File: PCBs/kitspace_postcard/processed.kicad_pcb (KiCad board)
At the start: 2 copper layers, 100 x 100 mm, 23 parts, among them SW1 SW_Push, U1 ATtiny85-20SU

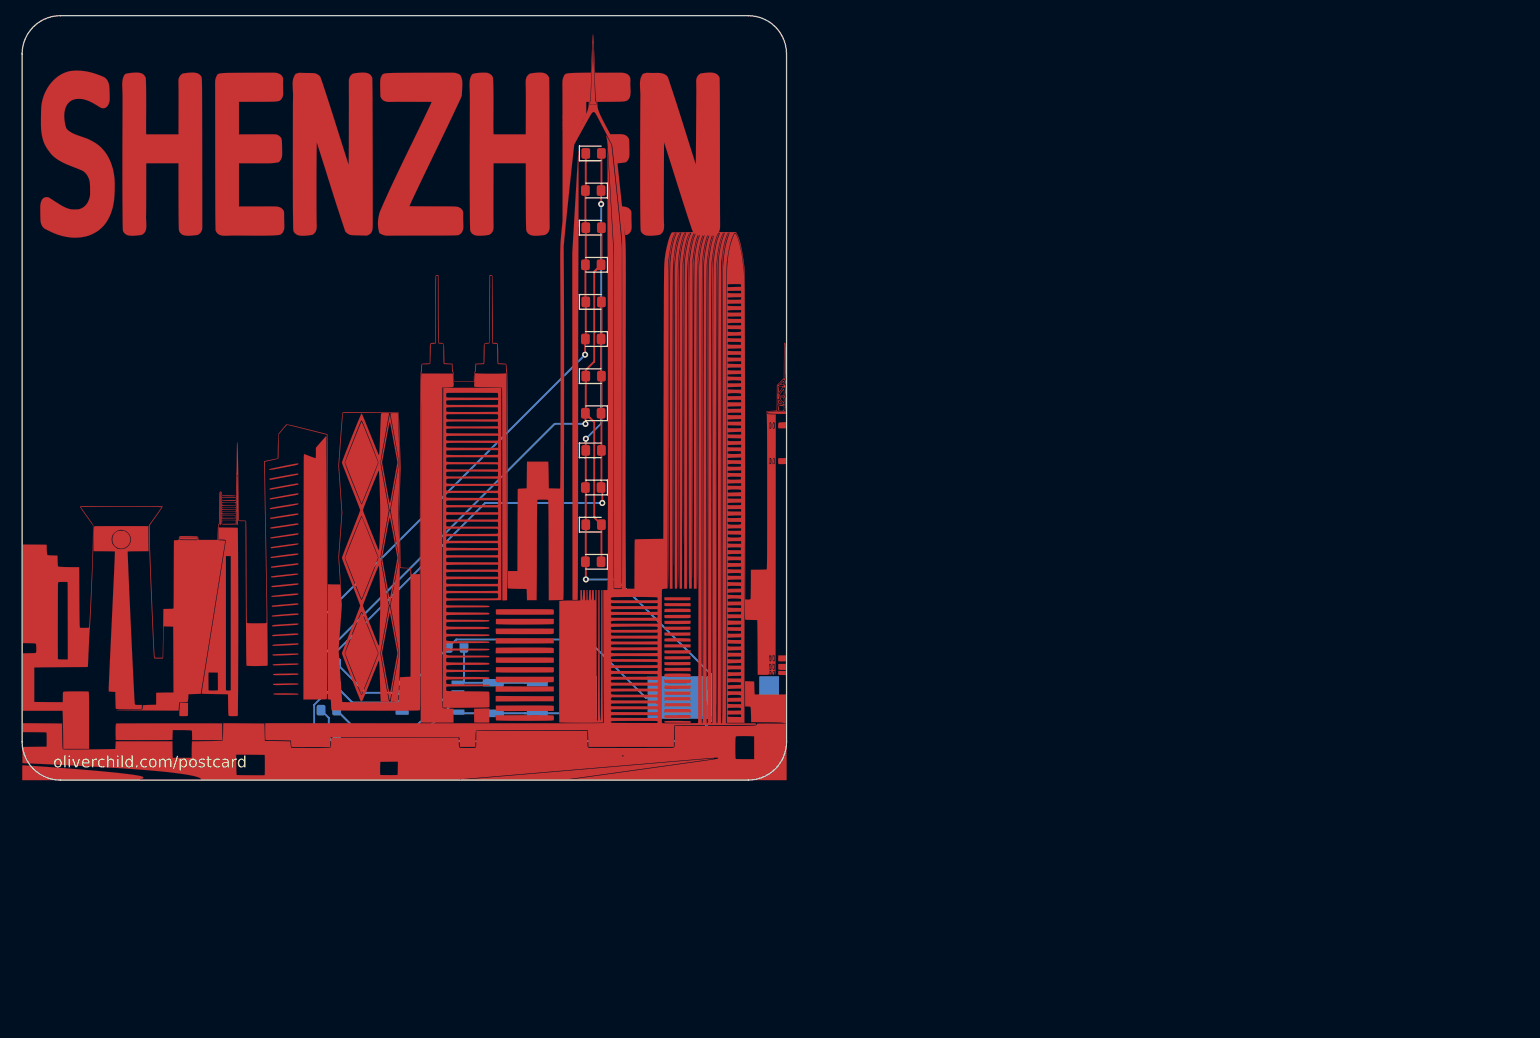
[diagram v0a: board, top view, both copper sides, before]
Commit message: recheck all circuits and clean up fill zone by rerouting the nets using freerouting and manually
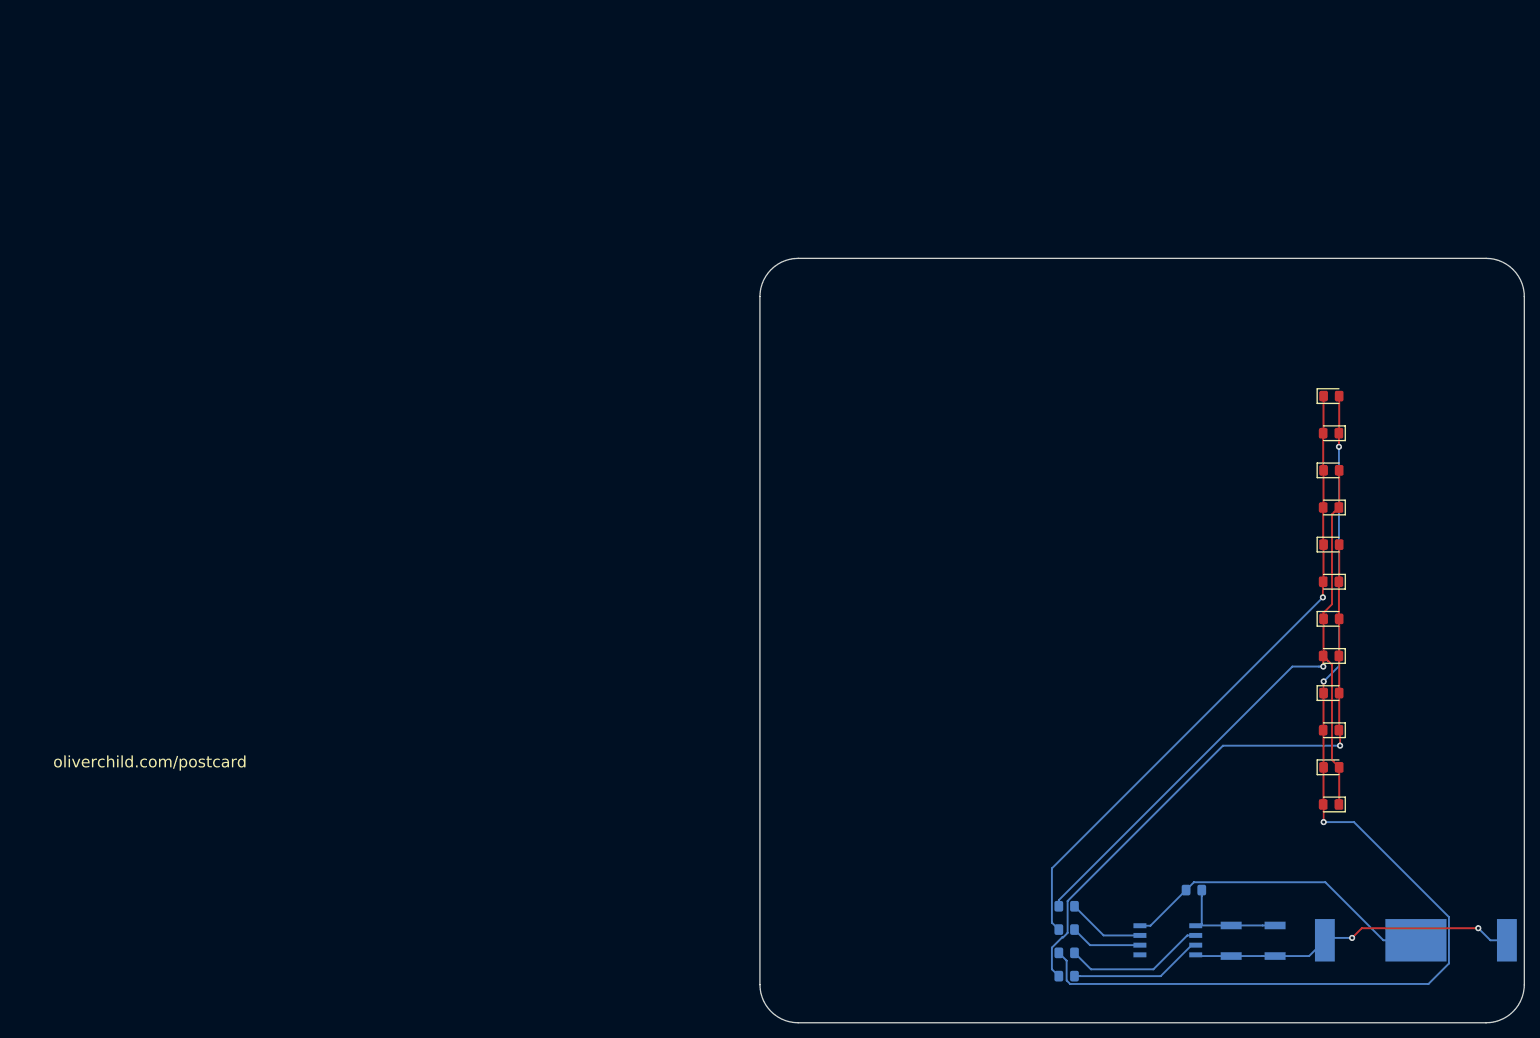
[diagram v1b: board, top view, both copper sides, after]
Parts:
- removed the G*** at (50.0, 50.0) (x2)
- moved D5 101.6 mm to (171.2, 74.1)
- moved D10 101.6 mm to (171.3, 98.3)
- moved D11 101.6 mm to (171.3, 78.9)
- moved D2 101.6 mm to (171.3, 69.2)
- moved D6 101.6 mm to (171.3, 59.5)
- moved D7 101.6 mm to (171.3, 49.8)
- moved SW1 101.6 mm to (161.0, 121.0)
- moved U1 101.6 mm to (149.9, 121.0)
- moved BT1 101.6 mm to (182.3, 121.0)
- moved D1 101.6 mm to (171.2, 93.5)
- moved D12 101.6 mm to (171.2, 83.8)
- moved D3 101.6 mm to (171.2, 64.3)
- moved D8 101.6 mm to (171.2, 54.6)
- moved D9 101.6 mm to (171.2, 103.2)
- moved R2 101.6 mm to (136.6, 122.6)
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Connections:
- U1 pad 1: (no net) -> Net-(U1-Pad1)
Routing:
- net VDD: track 17.8 -> 42.9 mm, vias 0 -> 2
